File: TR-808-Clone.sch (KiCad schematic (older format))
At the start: 577 parts, among them J1 BD, J10 OH, J11 CH, J12 MASTER, J2 SD, J3 LT, J4 MT, J5 HT, J6 RS, J7 CP, J8 CB, J9 CY, P1 CONN_02X05, P10 CONN_01X01, P11 CONN_01X01, P2 CONN_01X08, P4 CONN_01X01, P5 CONN_01X01, P8 CONN_01X01, P9 CONN_01X01, Q10 A733, Q11 C945, Q12 A733, Q13 J111/J112, Q27-1 C945, Q28 C945, Q29 A733, Q31 C945, Q32 C945, Q33 C945, Q34 C945, Q35 C945, Q36 C945, Q37 A733, Q39 C945, Q40 A733, Q41 C945, Q42 C945, Q43 C945, Q44 C945, Q45 C945, Q46 A733, Q47 C945, Q48 C945, Q49 C945, Q50 C945, Q51 A733, Q52 C945, Q53 C945, Q54 A733, Q55 C945, Q56 C945, Q57 A733, Q58 C945, Q59 C945, Q60 A733, Q61 C945, Q62 C945, Q63 C945, Q65 A733, Q66 A733, Q67 C945, Q68 C945, Q69 C945, Q70 C945, Q71 A733, Q72 A733, Q73 C945, Q74 J111/J112, U10 CD4053, U11 CD4053, U12 4558, U13 4558, U14 4558, U15 4558, U16 4558, U17 4558, U18 4558, U19 4558, U20 4558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

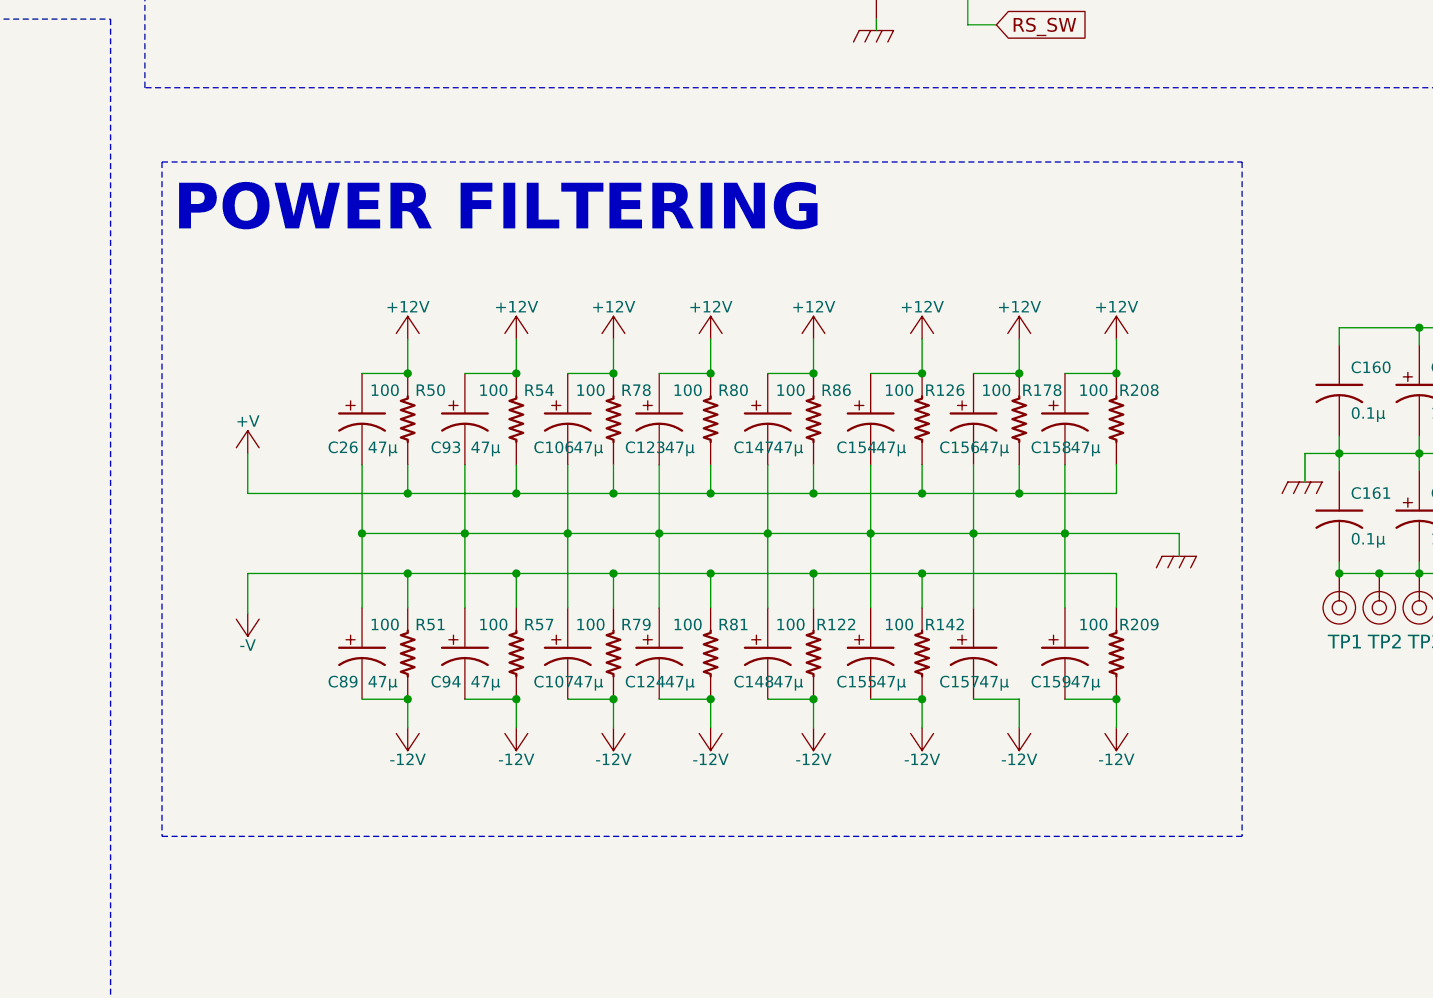
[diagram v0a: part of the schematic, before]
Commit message: added extra RC filter on mix out circuit
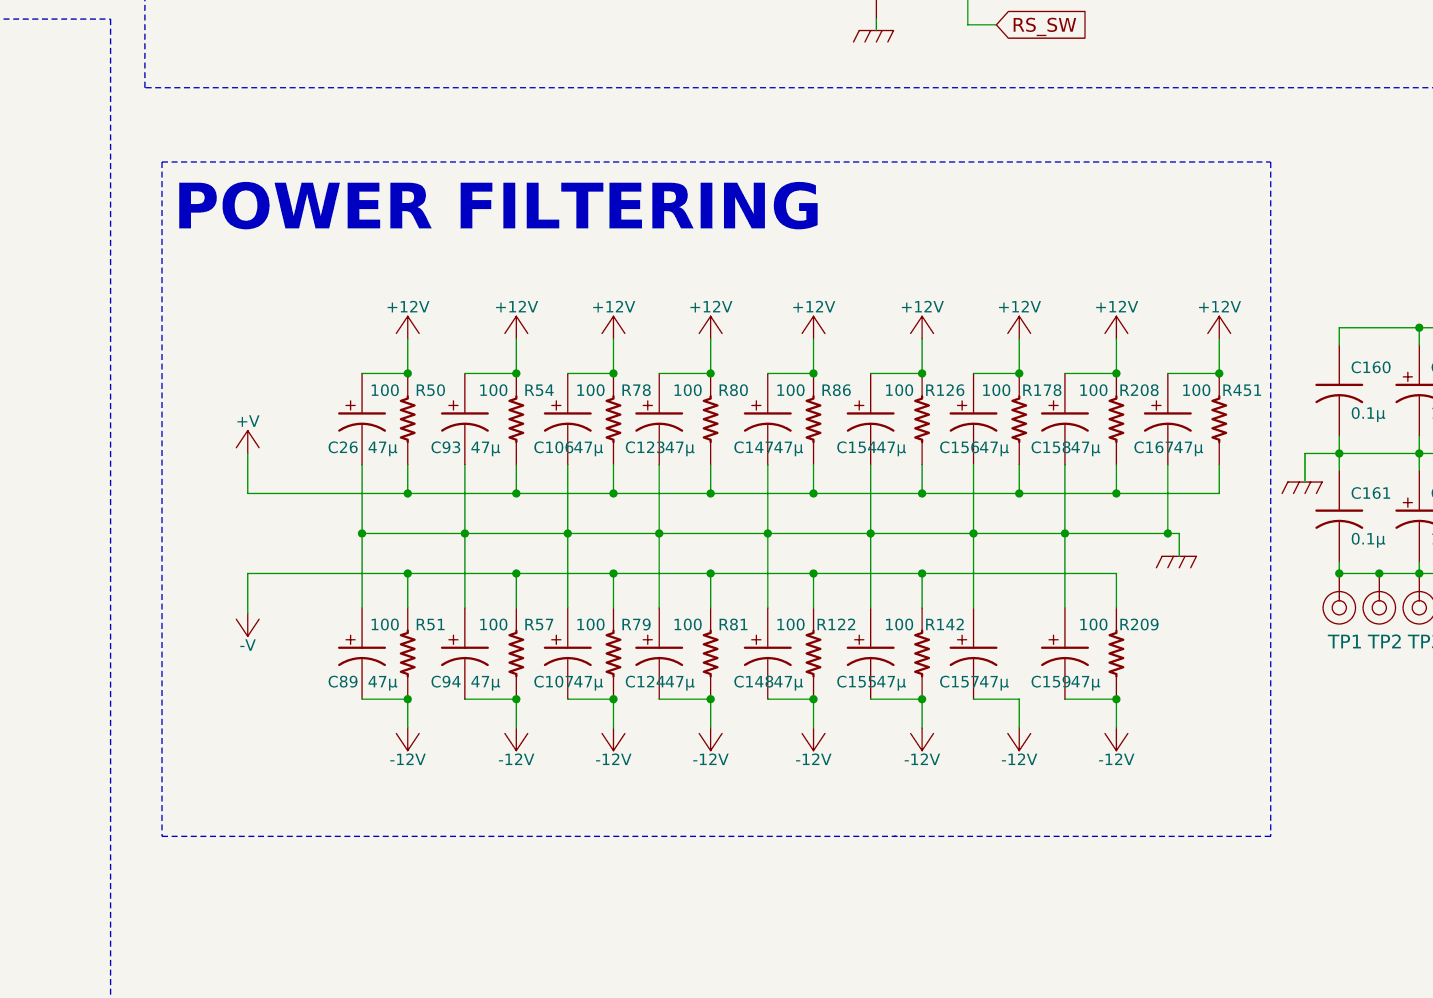
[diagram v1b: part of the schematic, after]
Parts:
- added C167: 47μ, MyModules:jrl_c_elec_5x5.3, symbol CP_US
- added R451: 100, MyModules:SM0603-R-JRL, symbol R_US
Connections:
- net +12V: now also C167.1 (+), R451.1
- net +V: now also R451.2
- net GND: now also C167.2 (-)

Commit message: adjusted bottom ground plane, completely split now. starting to change 12V names to account for RC isolation
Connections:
- net +12V: no longer C26.1 (+), C34-1.1 (+), Q44.3 (C), R102.1, R121.1, R156.2, R160.1, R50.1, R97.1, U12.8 (V+), U6.13, U6.14 (VDD), U6.9, VR3.3
- new net V1+: C26.1 (+), C34-1.1 (+), Q44.3 (C), R102.1, R121.1, R156.2, R160.1, R50.1, R97.1, U12.8 (V+), U6.13, U6.14 (VDD), U6.9, VR3.3
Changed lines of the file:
@@
 $EndComp
 $Comp
-L +12V #PWR039
-U 1 1 568C7559
-P 3550 1475
-F 0 "#PWR039" H 3550 1325 50  0001 C CNN
-F 1 "+12V" H 3550 1615 50  0000 C CNN
-F 2 "" H 3550 1475 60  0000 C CNN
-F 3 "" H 3550 1475 60  0000 C CNN
-	1    3550 1475
-	1    0    0    -1
-$EndComp
-$Comp
 L R_US R160
 U 1 1 568C7F18
@@
 $EndComp
 $Comp
-L +12V #PWR040
-U 1 1 568C84AA
-P 4250 1475
-F 0 "#PWR040" H 4250 1325 50  0001 C CNN
-F 1 "+12V" H 4250 1615 50  0000 C CNN
-F 2 "" H 4250 1475 60  0000 C CNN
-F 3 "" H 4250 1475 60  0000 C CNN
-	1    4250 1475
-	1    0    0    -1
-$EndComp
-$Comp
 L C_US C39
 U 1 1 568C9C38
@@
 $EndComp
 $Comp
-L +12V #PWR048
-U 1 1 568ED341
-P 9375 4125
-F 0 "#PWR048" H 9375 3975 50  0001 C CNN
-F 1 "+12V" H 9375 4265 50  0000 C CNN
-F 2 "" H 9375 4125 60  0000 C CNN
-F 3 "" H 9375 4125 60  0000 C CNN
-	1    9375 4125
-	1    0    0    -1
-$EndComp
-$Comp
 L R_US R173
 U 1 1 568EDA06
@@
 $EndComp
 $Comp
-L +12V #PWR068
-U 1 1 56947EF8
-P 5550 4175
-F 0 "#PWR068" H 5550 4025 50  0001 C CNN
-F 1 "+12V" H 5550 4315 50  0000 C CNN
-F 2 "" H 5550 4175 60  0000 C CNN
-F 3 "" H 5550 4175 60  0000 C CNN
-	1    5550 4175
-	1    0    0    -1
-$EndComp
-$Comp
 L -12V #PWR069
 U 1 1 56947EFE
@@
 	22700 11825 22700 11925
 $Comp
-L +12V #PWR0184
-U 1 1 5705C0DF
-P 22700 11425
-F 0 "#PWR0184" H 22700 11275 50  0001 C CNN
-F 1 "+12V" H 22700 11565 50  0000 C CNN
-F 2 "" H 22700 11425 60  0000 C CNN
-F 3 "" H 22700 11425 60  0000 C CNN
-	1    22700 11425
-	1    0    0    -1
-$EndComp
-$Comp
 L R_US R112
 U 1 1 570714B0
@@
 	1    0    0    1
 $EndComp
-$Comp
-L +12V #PWR0186
-U 1 1 57085B18
-P 23225 8600
-F 0 "#PWR0186" H 23225 8450 50  0001 C CNN
-F 1 "+12V" H 23225 8740 50  0000 C CNN
-F 2 "" H 23225 8600 60  0000 C CNN
-F 3 "" H 23225 8600 60  0000 C CNN
-	1    23225 8600
-	1    0    0    -1
-$EndComp
 Wire Wire Line
 	23225 8600 23225 8650
-$Comp
-L +12V #PWR0187
-U 1 1 5708F86F
-P 23375 10550
-F 0 "#PWR0187" H 23375 10400 50  0001 C CNN
-F 1 "+12V" H 23375 10690 50  0000 C CNN
-F 2 "" H 23375 10550 60  0000 C CNN
-F 3 "" H 23375 10550 60  0000 C CNN
-	1    23375 10550
-	1    0    0    -1
-$EndComp
 Wire Wire Line
 	23375 10550 23375 10900
@@
 	1    0    0    -1
 $EndComp
-$Comp
-L +12V #PWR0189
-U 1 1 570AEEDB
-P 25475 10375
-F 0 "#PWR0189" H 25475 10225 50  0001 C CNN
-F 1 "+12V" H 25475 10515 50  0000 C CNN
-F 2 "" H 25475 10375 60  0000 C CNN
-F 3 "" H 25475 10375 60  0000 C CNN
-	1    25475 10375
-	1    0    0    -1
-$EndComp
 Wire Wire Line
 	25475 10775 25475 11000
 Connection ~ 25475 11000
-$Comp
-L +12V #PWR0190
-U 1 1 570B9018
-P 25975 10375
-F 0 "#PWR0190" H 25975 10225 50  0001 C CNN
-F 1 "+12V" H 25975 10515 50  0000 C CNN
-F 2 "" H 25975 10375 60  0000 C CNN
-F 3 "" H 25975 10375 60  0000 C CNN
-	1    25975 10375
-	1    0    0    -1
-$EndComp
 Wire Wire Line
 	25975 10375 25975 10800
@@
 	1    0    0    -1
 $EndComp
-$Comp
-L +12V #PWR0195
-U 1 1 57101500
-P 26325 8250
-F 0 "#PWR0195" H 26325 8100 50  0001 C CNN
-F 1 "+12V" H 26325 8390 50  0000 C CNN
-F 2 "" H 26325 8250 60  0000 C CNN
-F 3 "" H 26325 8250 60  0000 C CNN
-	1    26325 8250
-	1    0    0    -1
-$EndComp
 Wire Wire Line
 	27525 9375 27525 9450
@@
 Wire Wire Line
 	29200 8750 29200 8800
-$Comp
-L +12V #PWR0199
-U 1 1 5713F06D
-P 29850 7575
-F 0 "#PWR0199" H 29850 7425 50  0001 C CNN
-F 1 "+12V" H 29850 7715 50  0000 C CNN
-F 2 "" H 29850 7575 60  0000 C CNN
-F 3 "" H 29850 7575 60  0000 C CNN
-	1    29850 7575
-	1    0    0    -1
-$EndComp
 Connection ~ 29850 7800
 Text GLabel 30125 8775 2    60   Output ~ 0
@@
 $EndComp
 $Comp
-L +12V #PWR0231
-U 1 1 56F23044
-P 11925 14625
-F 0 "#PWR0231" H 11925 14475 50  0001 C CNN
-F 1 "+12V" H 11925 14765 50  0000 C CNN
-F 2 "" H 11925 14625 60  0000 C CNN
-F 3 "" H 11925 14625 60  0000 C CNN
-	1    11925 14625
-	1    0    0    -1
-$EndComp
-$Comp
 L -12V #PWR0232
 U 1 1 56F2304A
@@
 	15475 15300 15475 15175
 Connection ~ 15025 15300
+Text Label 11925 14625 0    60   ~ 0
+V1+
+Text Label 26325 8250 0    60   ~ 0
+V1+
+Text Label 29850 7575 0    60   ~ 0
+V1+
+Text Label 25975 10375 0    60   ~ 0
+V1+
+Text Label 25475 10375 0    60   ~ 0
+V1+
+Text Label 23375 10550 0    60   ~ 0
+V1+
+Text Label 22700 11425 0    60   ~ 0
+V1+
+Text Label 23225 8600 0    60   ~ 0
+V1+
+Text Label 4250 1475 0    60   ~ 0
+V1+
+Text Label 3550 1475 0    60   ~ 0
+V1+
+Text Label 5550 4175 0    60   ~ 0
+V1+
+Text Label 9375 4125 0    60   ~ 0
+V1+
 $EndSCHEMATC

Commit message: updated rail labelling 0 unconnected with new labelling
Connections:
- net V1+: now also R237.1
- removed net +12V: C106.1 (+), C123.1 (+), C147.1 (+), C154.1 (+), C156.1 (+), C158.1 (+), C167.1 (+), C93.1 (+), D9.1 (K), Q49.3 (C), Q63.3 (C), Q65.2 (E), Q68.3 (C), Q69.3 (C), R124.1, R126.1, R178.1, R193.1, R194.2, R208.1, R221.1, R237.1, R252.1, R279.1, R321.2, R343.2, R363.1, R366.2, R451.1, R54.1, R78.1, R80.1, R86.1, U13.8 (V+), U14.8 (V+), U15.8 (V+), U16.8 (V+), U17.8 (V+), U18.8 (V+), U19.8 (V+), U20.8 (V+), U21.8 (V+), U24.8 (V+), U4.8 (V+)
- removed net -12V: C107.2 (-), C124.2 (-), C148.2 (-), C155.2 (-), C157.2 (-), C159.2 (-), C7.2 (-), C8.2 (-), C89.2 (-), C94.2 (-), D10.2 (A), D70.2 (A), Q11.2 (E), Q61.2 (E), Q72.3 (C), Q73.2 (E), R122.2, R142.2, R173.1, R200-1.2, R203.1, R209.2, R304.1, R323.1, R347.2, R351.2, R361.2, R51.2, R57.2, R69.1, R79.2, R81.2, TM3.3, U10.7 (Vee), U11.7 (Vee), U12.4 (V-), U13.4 (V-), U14.4 (V-), U15.4 (V-), U16.4 (V-), U17.4 (V-), U18.4 (V-), U19.4 (V-), U20.4 (V-), U21.4 (V-), U23.12 (GND), U24.4 (V-), U25.7 (Vee), U26.7 (Vee), U4.4 (V-)
- new net V1-: C89.2 (-), R173.1, R51.2, U12.4 (V-)
- new net V2+: C93.1 (+), Q49.3 (C), R193.1, R194.2, R54.1, U13.8 (V+), U14.8 (V+)
- new net V2-: C94.2 (-), R203.1, R57.2, U13.4 (V-), U14.4 (V-)
- new net V3+: C106.1 (+), R221.1, R78.1, U15.8 (V+)
- new net V3-: C107.2 (-), R79.2, U10.7 (Vee), U15.4 (V-), U16.4 (V-), U17.4 (V-), U24.4 (V-), U25.7 (Vee)
- new net V4+: C123.1 (+), R124.1, R252.1, R279.1, R80.1, U16.8 (V+), U17.8 (V+), U18.8 (V+), U24.8 (V+)
- new net V4-: C124.2 (-), Q61.2 (E), Q72.3 (C), R304.1, R323.1, R81.2, U11.7 (Vee), U18.4 (V-), U19.4 (V-), U20.4 (V-), U21.4 (V-), U26.7 (Vee)
- new net V5+: C147.1 (+), Q63.3 (C), R321.2, R363.1, R366.2, R86.1, U20.8 (V+), U21.8 (V+)
- new net V5-: C148.2 (-), D70.2 (A), Q73.2 (E), R122.2, R200-1.2, R347.2, R351.2, R361.2, TM3.3, U23.12 (GND)
- new net V6+: C156.1 (+), Q68.3 (C), Q69.3 (C), R178.1, R343.2, U19.8 (V+)
- new net V6-: C155.2 (-), R142.2
- new net V7+: C154.1 (+), Q65.2 (E), R126.1
- new net V7-: C157.2 (-), C159.2 (-), C7.2 (-), C8.2 (-), D10.2 (A), Q11.2 (E), R209.2, R69.1, U4.4 (V-)
- new net V8+: C158.1 (+), R208.1
- new net V9+: C167.1 (+), D9.1 (K), R451.1, U4.8 (V+)

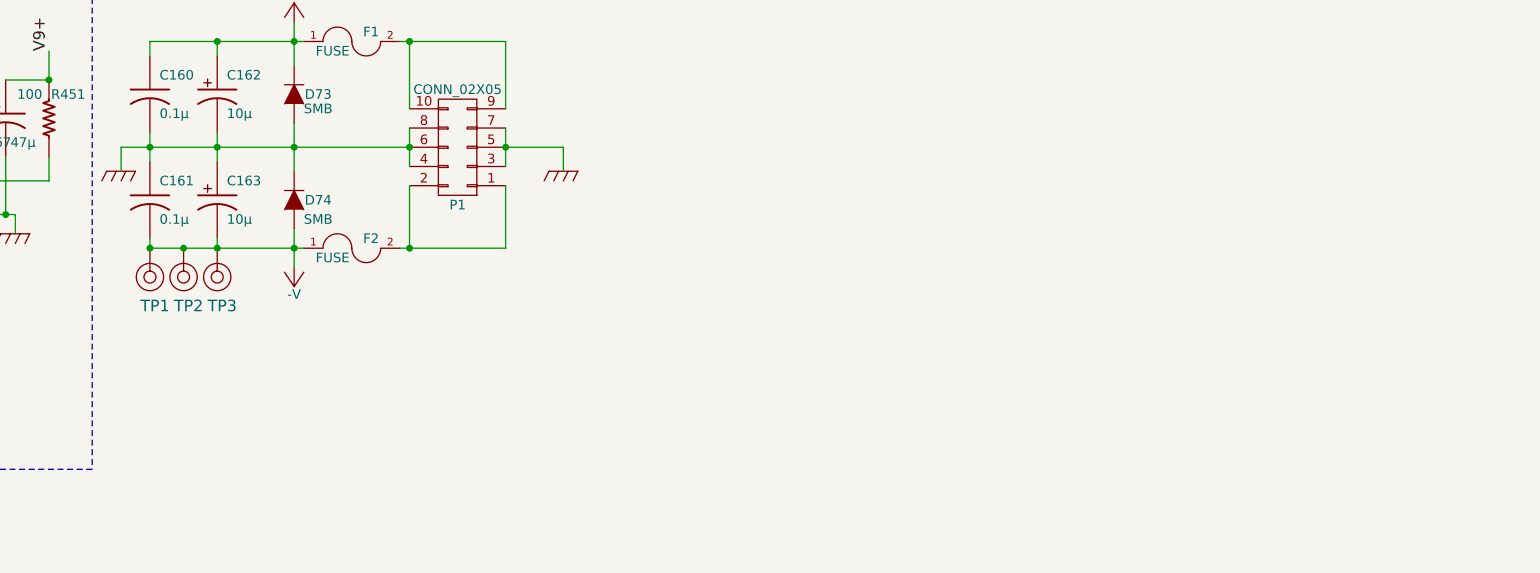
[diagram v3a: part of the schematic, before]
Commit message: added larger bypass caps to switch board, adding coupling caps to critical op amps
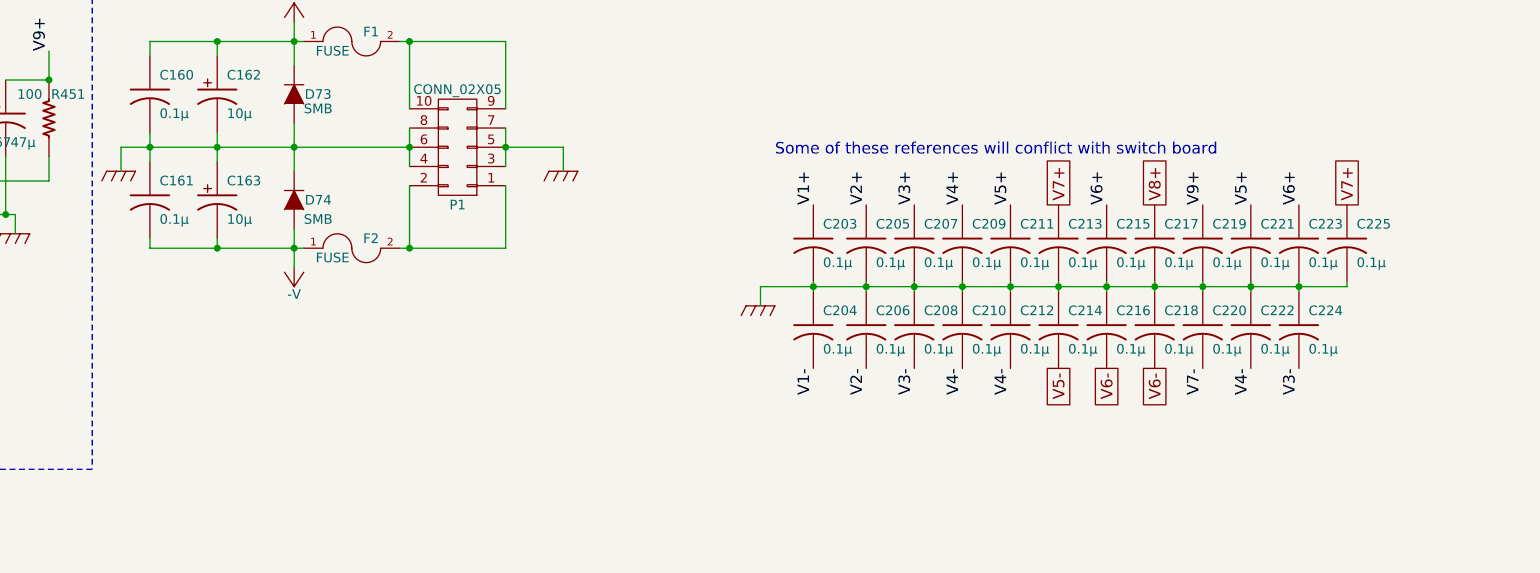
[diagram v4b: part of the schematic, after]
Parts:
- removed TP1, TP2, TP3: TEST_POINT, Pin_Headers:Pin_Header_Straight_1x01_Pitch2.54mm, symbol TEST_POINT
- added C203, C204, C205, C206, C207, C208, C209, C210, C211, C212, C213, C214, C215, C216, C217, C218, C219, C220, C221, C222, C223, C224, C225: 0.1μ, MyModules:SM0603-C-JRL, symbol C_US
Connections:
- net GND: now also C203.2, C204.1, C205.2, C206.1, C207.2, C208.1, C209.2, C210.1, C211.2, C212.1, C213.2, C214.1, C215.2, C216.1, C217.2, C218.1, C219.2, C220.1, C221.2, C222.1, C223.2, C224.1, C225.2
- net V1+: now also C203.1
- net V1-: now also C204.2
- net V2+: now also C205.1
- net V2-: now also C206.2
- net V3+: now also C207.1
- net V3-: now also C208.2, C224.2
- net V4+: now also C209.1
- net V4-: now also C210.2, C212.2, C222.2
- net V5+: now also C211.1, C221.1
- net V5-: now also C214.2
- net V6+: now also C215.1, C223.1
- net V6-: now also C216.2, C218.2
- net V7+: now also C213.1, C225.1
- net V7-: now also C220.2
- net V8+: now also C217.1
- net V9+: now also C219.1
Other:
- note added: "Some of these references will conflict with switch board"

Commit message: added ferrite beads on rail inputs, routed
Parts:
- added L3, L4: BEAD, MyModules:SM0805-HAND, symbol INDUCTOR
- C162, C163: value 10µ -> 47µ
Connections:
- net at P1.1 (P1), P1.2 (P2): now also L4.2; no longer F2.2
- net at P1.10 (P10), P1.9 (P9): now also L3.2; no longer F1.2
- new net: F1.2, L3.1
- new net: F2.2, L4.1
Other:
- moved on the sheet: P1

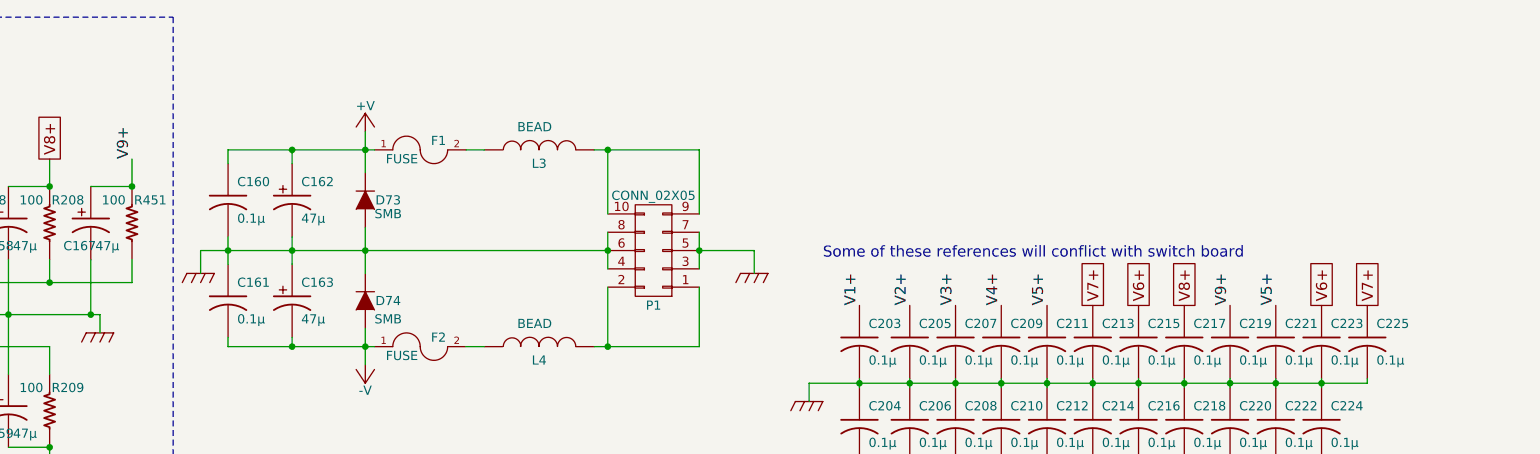
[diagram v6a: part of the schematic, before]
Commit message: fixed duplicate reference between main board and switch board
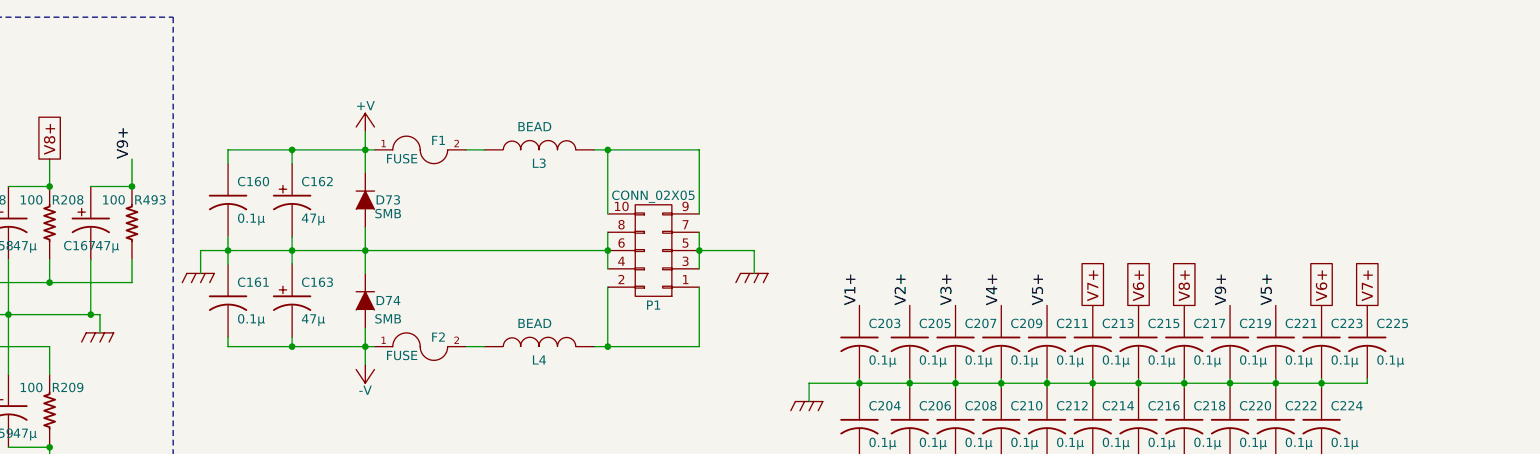
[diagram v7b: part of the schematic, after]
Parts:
- renumbered R451 to R493
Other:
- note removed: "Some of these references will conflict with switch board"
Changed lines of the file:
@@
 $EndComp
 $Comp
-L R_US R451
+L R_US R493
 U 1 1 5AEC28BB
 P 15475 14975
-F 0 "R451" H 15575 15100 50  0000 C CNN
+F 0 "R493" H 15575 15100 50  0000 C CNN
 F 1 "100" H 15375 15100 50  0000 C CNN
 F 2 "MyModules:SM0603-R-JRL" H 15475 14975 60  0001 C CNN
@@
 Text Notes 17775 10325 0    60   ~ 0
 C126 has WRONG\nfootprint - need to\nenlarge- CHANGED\nTO 5.3MM
-Text Notes 19250 15175 0    60   ~ 0
-Some of these references will conflict with switch board
 $Comp
 L C_US C219
